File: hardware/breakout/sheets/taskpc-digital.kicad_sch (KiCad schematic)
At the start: 63 parts, among them J2 Connector 0 (analog + AISENSE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, J3 Connector 1 (digital, task PC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, J4 Manual reward button (panel), J5 Remote reward jack (parallel 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, J6 Reward driver out (BNC, place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, U10 SN74HCT541PW, U11 SN74HCT541PW, U12 SN74HCT32D, U13 SN74HCT14D, U5 SN74LVC541APW, U6 SN74LVC541APW, U7 SN74LVC541APW, U8 SN74HCT541PW, U9 SN74HCT541PW

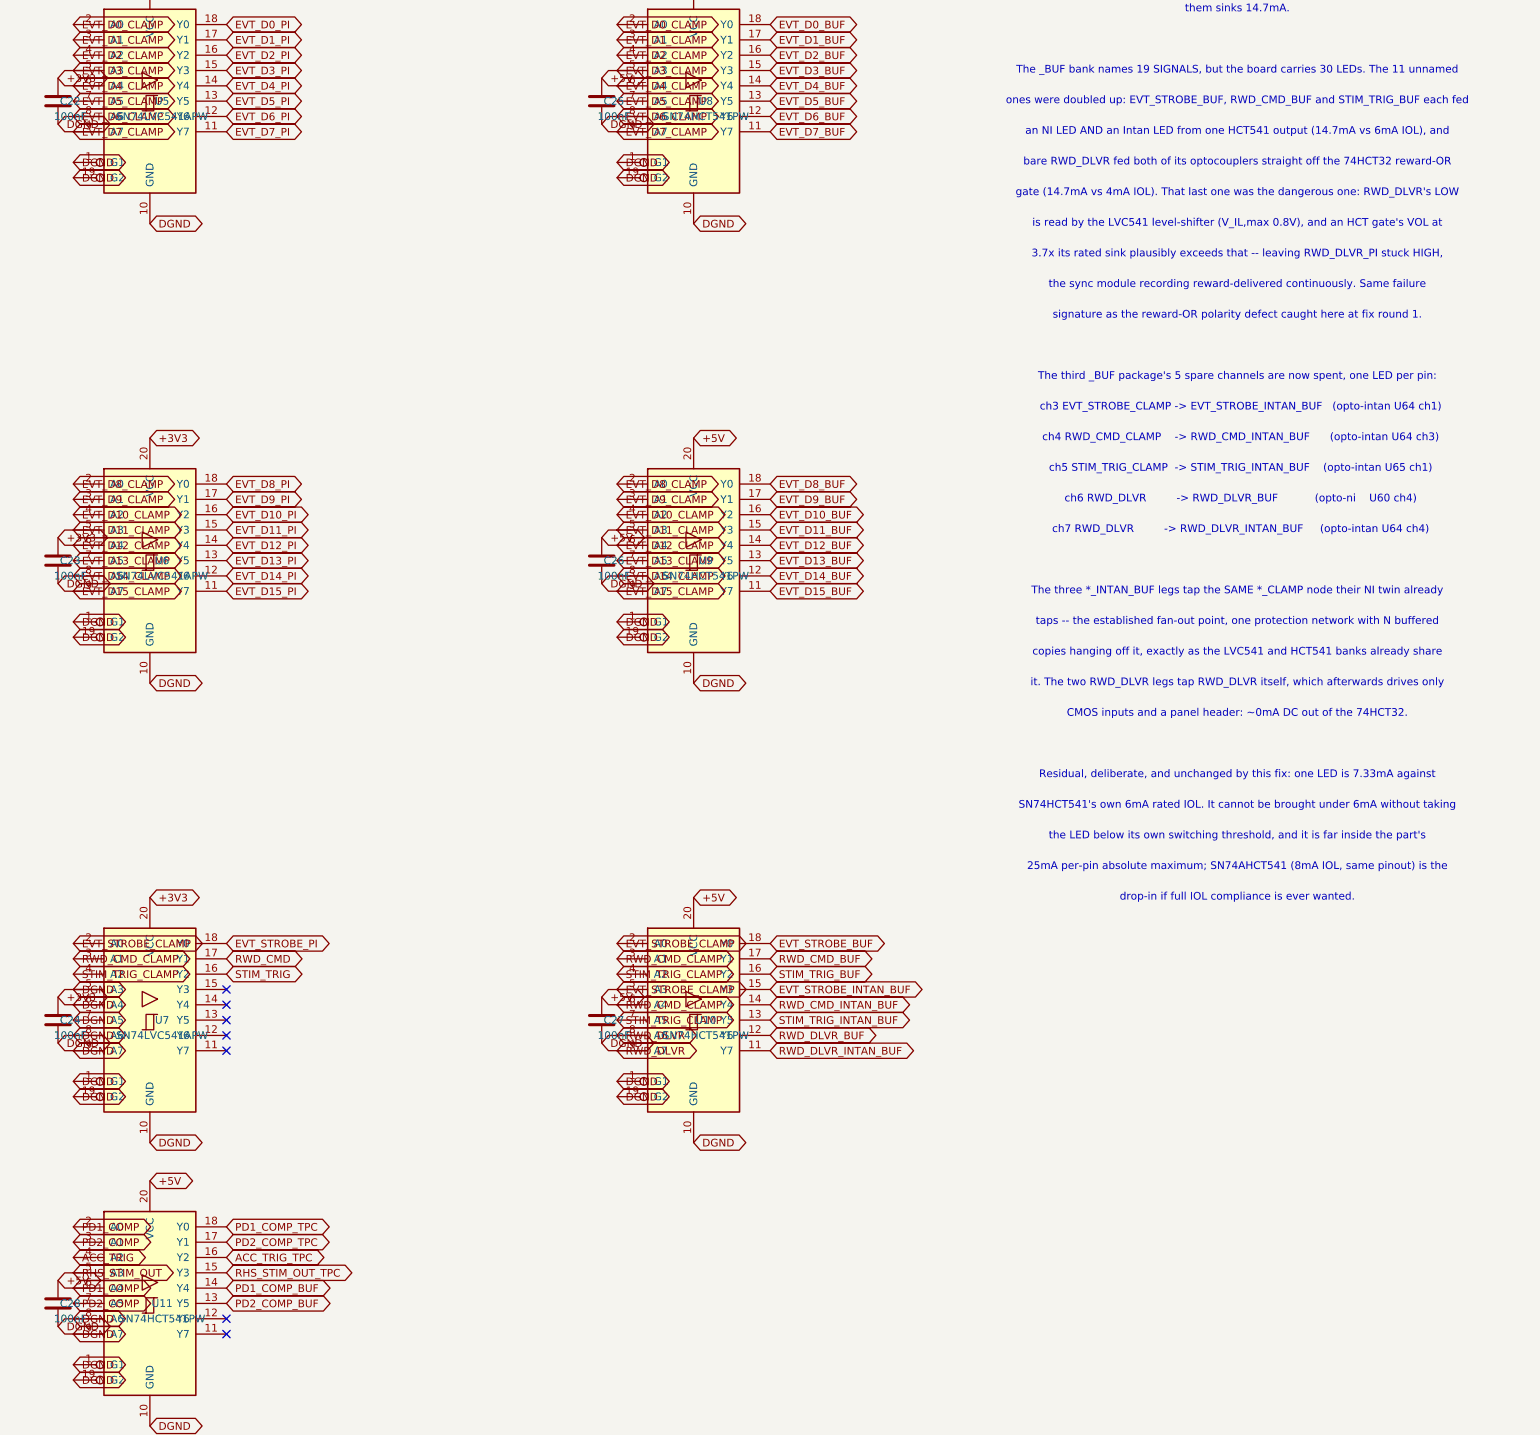
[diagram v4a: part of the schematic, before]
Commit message: fix(hw): swap SN74AHCT541PW in for SN74HCT541PW on U8-U11, U15
Each of these five packages drives exactly one ACSL-6400/6420 LED at
~7.33mA, fixed by the LED's own 7.0mA worst-case switching threshold,
not a driver choice. SN74HCT541PW is rated IOL=6mA: 7.33mA is 22% over
the rated sink -- far inside the part's 25mA per-pin absolute maximum,
but past its guaranteed-VOL condition, and the prior report's own
"22% over, bounded" framing was self-inconsistent: it applied the
datasheet VOL figure quoted at the rated 6mA to a 7.33mA load. Solved
self-consistently against the part's own ~55 ohm output impedance (not
the single 6mA test point), the real current is closer to 7.18mA --
uncomfortably close to the LED's own 7.0mA floor, and below it at V_F
max with the 5V rail 5% low. Running out of spec was eroding exactly
the margin the out-of-spec operation was meant to buy.

SN74AHCT541PW is rated IOL=8mA (identical pinout, identical TSSOP-20
footprint, same 74xx:74LS541-derived KiCad symbol family), making
7.33mA fully compliant with margin, and doubles both absolute maxima
(25mA->50mA/pin, 70mA->100mA/package) -- retiring the separate concern
that U8/U9/U10 sat at 58.6mA of a 70mA package limit.

Confirmed to be exactly what it should be: a Value/MPN edit on five
refdes, zero refdes churn, no footprint change. Diffing the whole
board's own component list (netlist-contract.json) against the prior
commit shows only U8/U9/U10/U11/U15 changing Value, nothing else added,
removed, or renumbered.

check_taskpc_digital_netlist.py and check_breakout_pi_interface_netlist.py
updated to expect the new Value on these exact five references (both
files independently redefine their own contract rather than importing
the generator's, so both needed the literal string updated); the "one
LED per driver pin" invariant they enforce is unaffected -- doubling up
would still overload the new part's own 8mA rating just as surely.

AHCT's faster edges are a layout-stage concern, not a schematic-ca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
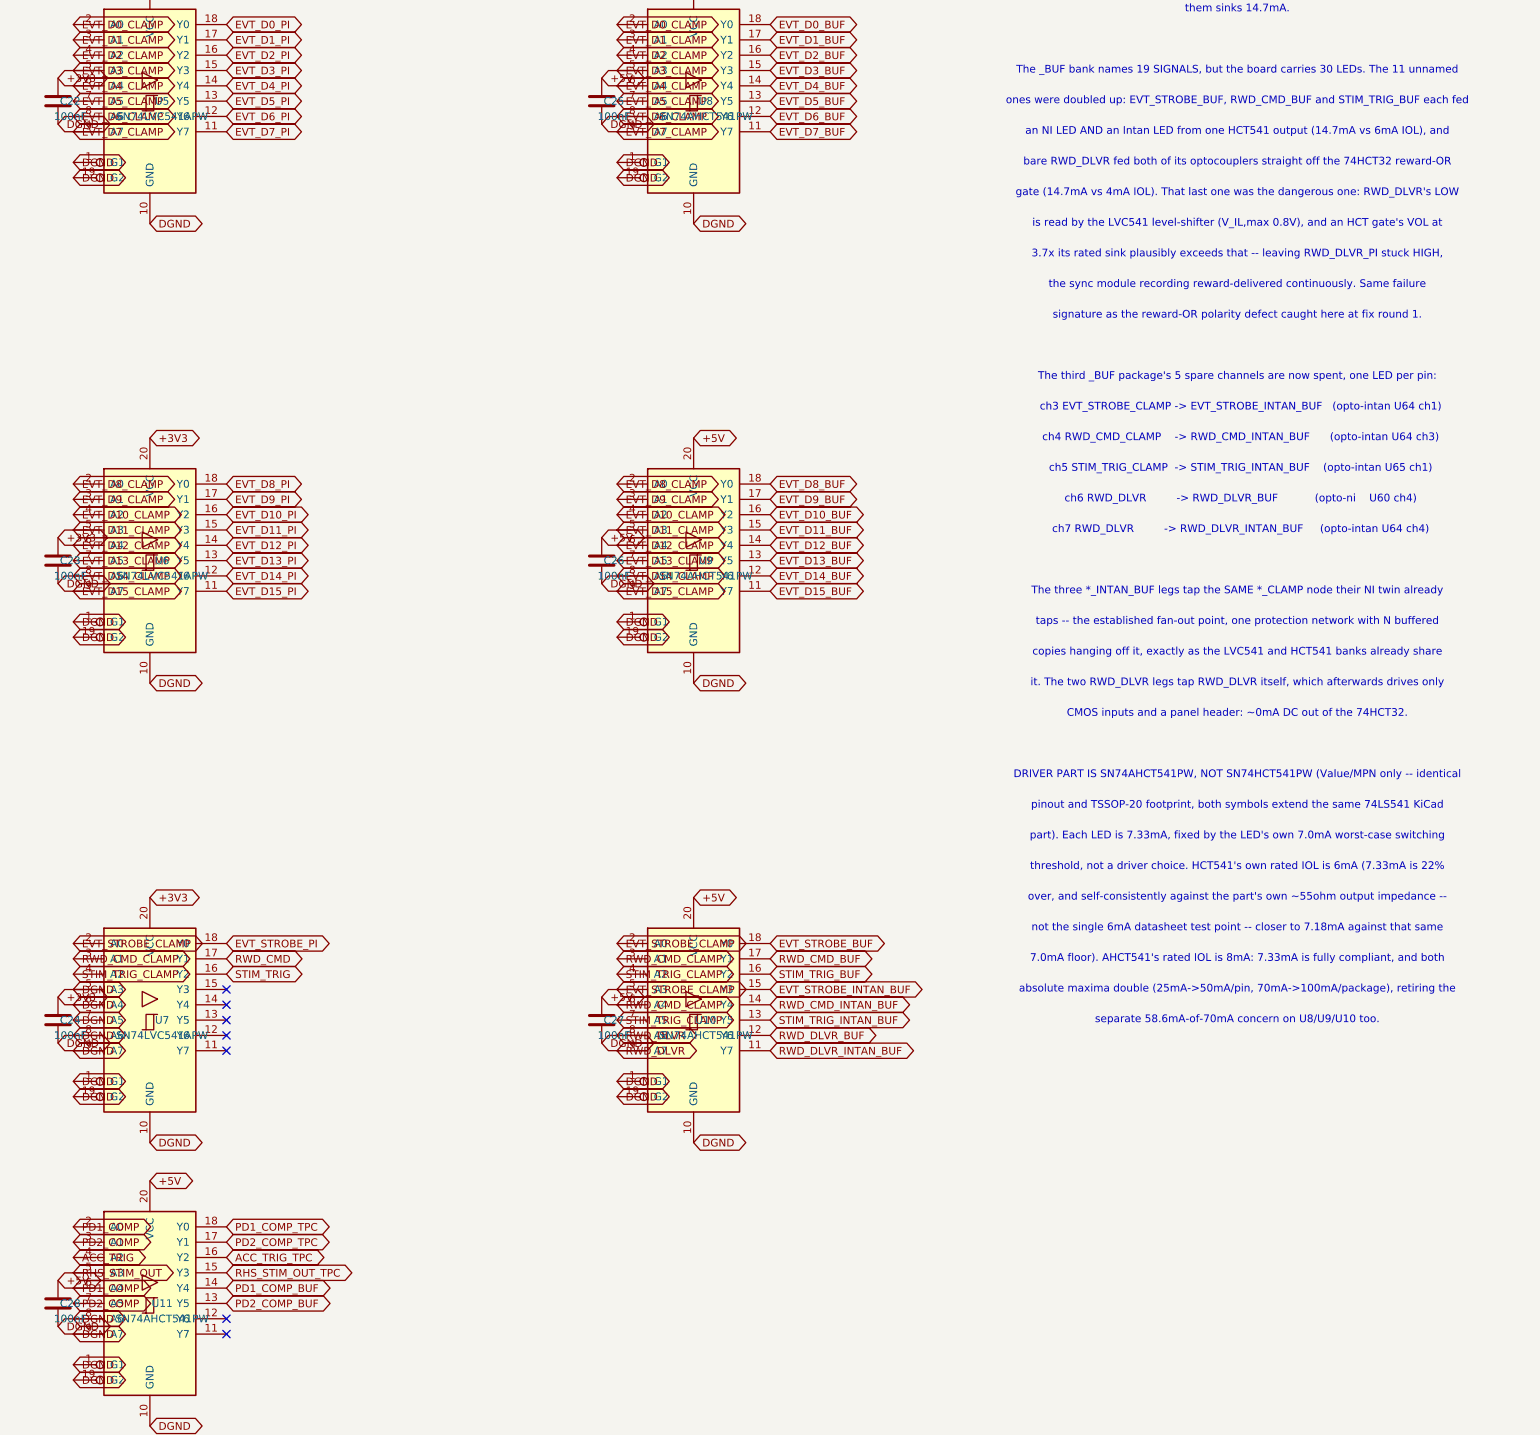
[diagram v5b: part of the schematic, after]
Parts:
- removed U10, U11, U8, U9: SN74HCT541PW, Package_SO:Texas_PW0020A_TSSOP-20_4.4x6.5mm_P0.65mm, symbol 74xx:74HCT541
- added U10, U11, U8, U9: SN74AHCT541PW, Package_SO:Texas_PW0020A_TSSOP-20_4.4x6.5mm_P0.65mm, symbol 74xx:74AHCT541
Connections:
- net +5V: now also U10.20 (VCC), U11.20 (VCC), U8.20 (VCC), U9.20 (VCC)
- net ACC_TRIG: now also U11.4 (A2)
- net ACC_TRIG_TPC: now also U11.16 (Y2)
- net DGND: now also U10.1 (G1), U10.10 (GND), U10.19 (G2), U11.1 (G1), U11.10 (GND), U11.19 (G2), U11.8 (A6), U11.9 (A7), U8.1 (G1), U8.10 (GND), U8.19 (G2), U9.1 (G1), U9.10 (GND), U9.19 (G2)
- net EVT_D0_BUF: now also U8.18 (Y0)
- net EVT_D0_CLAMP: now also U8.2 (A0)
- net EVT_D10_BUF: now also U9.16 (Y2)
- net EVT_D10_CLAMP: now also U9.4 (A2)
- net EVT_D11_BUF: now also U9.15 (Y3)
- net EVT_D11_CLAMP: now also U9.5 (A3)
- net EVT_D12_BUF: now also U9.14 (Y4)
- net EVT_D12_CLAMP: now also U9.6 (A4)
- net EVT_D13_BUF: now also U9.13 (Y5)
- net EVT_D13_CLAMP: now also U9.7 (A5)
- net EVT_D14_BUF: now also U9.12 (Y6)
- net EVT_D14_CLAMP: now also U9.8 (A6)
- net EVT_D15_BUF: now also U9.11 (Y7)
- net EVT_D15_CLAMP: now also U9.9 (A7)
- net EVT_D1_BUF: now also U8.17 (Y1)
- net EVT_D1_CLAMP: now also U8.3 (A1)
- net EVT_D2_BUF: now also U8.16 (Y2)
- net EVT_D2_CLAMP: now also U8.4 (A2)
- net EVT_D3_BUF: now also U8.15 (Y3)
- net EVT_D3_CLAMP: now also U8.5 (A3)
- net EVT_D4_BUF: now also U8.14 (Y4)
- net EVT_D4_CLAMP: now also U8.6 (A4)
- net EVT_D5_BUF: now also U8.13 (Y5)
- net EVT_D5_CLAMP: now also U8.7 (A5)
- net EVT_D6_BUF: now also U8.12 (Y6)
- net EVT_D6_CLAMP: now also U8.8 (A6)
- net EVT_D7_BUF: now also U8.11 (Y7)
- net EVT_D7_CLAMP: now also U8.9 (A7)
- net EVT_D8_BUF: now also U9.18 (Y0)
- net EVT_D8_CLAMP: now also U9.2 (A0)
- net EVT_D9_BUF: now also U9.17 (Y1)
- net EVT_D9_CLAMP: now also U9.3 (A1)
- net EVT_STROBE_BUF: now also U10.18 (Y0)
- net EVT_STROBE_CLAMP: now also U10.2 (A0), U10.5 (A3)
- net EVT_STROBE_INTAN_BUF: now also U10.15 (Y3)
- net PD1_COMP: now also U11.2 (A0), U11.6 (A4)
- net PD1_COMP_BUF: now also U11.14 (Y4)
- net PD1_COMP_TPC: now also U11.18 (Y0)
- net PD2_COMP: now also U11.3 (A1), U11.7 (A5)
- net PD2_COMP_BUF: now also U11.13 (Y5)
- net PD2_COMP_TPC: now also U11.17 (Y1)
- net RHS_STIM_OUT: now also U11.5 (A3)
- net RHS_STIM_OUT_TPC: now also U11.15 (Y3)
- net RWD_CMD_BUF: now also U10.17 (Y1)
- net RWD_CMD_CLAMP: now also U10.3 (A1), U10.6 (A4)
- net RWD_CMD_INTAN_BUF: now also U10.14 (Y4)
- net RWD_DLVR: now also U10.8 (A6), U10.9 (A7)
- net RWD_DLVR_BUF: now also U10.12 (Y6)
- net RWD_DLVR_INTAN_BUF: now also U10.11 (Y7)
- net STIM_TRIG_BUF: now also U10.16 (Y2)
- net STIM_TRIG_CLAMP: now also U10.4 (A2), U10.7 (A5)
- net STIM_TRIG_INTAN_BUF: now also U10.13 (Y5)
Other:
- note added: "7.0mA floor). AHCT541's rated IOL is 8mA: 7.33mA is fully compliant, and both"
- note added: "DRIVER PART IS SN74AHCT541PW, NOT SN74HCT541PW (Value/MPN only -- identical"
- note added: "absolute maxima double (25mA->50mA/pin, 70mA->100mA/package), retiring the"
- note added: "not the single 6mA datasheet test point -- closer to 7.18mA against that same"
- note added: "over, and self-consistently against the part's own ~55ohm output impedance --"
- note added: "part). Each LED is 7.33mA, fixed by the LED's own 7.0mA worst-case switching"
- note added: "pinout and TSSOP-20 footprint, both symbols extend the same 74LS541 KiCad"
- note added: "separate 58.6mA-of-70mA concern on U8/U9/U10 too."
- note added: "threshold, not a driver choice. HCT541's own rated IOL is 6mA (7.33mA is 22%"
- note removed: "25mA per-pin absolute maximum; SN74AHCT541 (8mA IOL, same pinout) is the"
- note removed: "Residual, deliberate, and unchanged by this fix: one LED is 7.33mA against"
- note removed: "SN74HCT541's own 6mA rated IOL. It cannot be brought under 6mA without taking"
- note removed: "drop-in if full IOL compliance is ever wanted."
- note removed: "the LED below its own switching threshold, and it is far inside the part's"
